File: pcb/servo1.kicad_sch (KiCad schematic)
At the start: 34 parts, among them J1 Feeder 1, J10 Feeder 10, J11 Feeder 11, J12 Feeder 12, J13 Feeder 13, J14 Feeder 14, J15 Feeder 15, J16 Feeder 16, J2 Feeder 2, J3 Feeder 3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

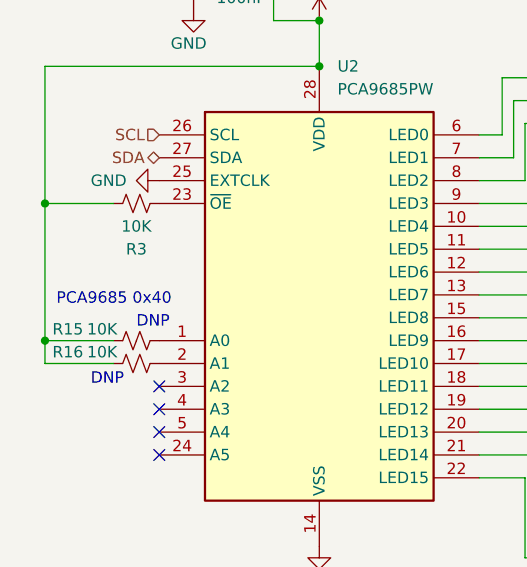
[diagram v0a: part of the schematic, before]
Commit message: Exclude R3 and R9 from population.
Upgrades files to KiCad 7.x.

Fixes: https://github.com/atanisoft/Esp32FeederController/issues/10
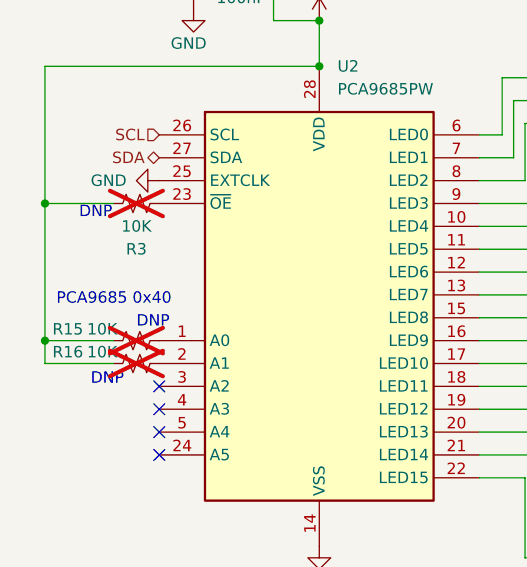
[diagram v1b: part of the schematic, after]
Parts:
- R15, R16, R3: now not fitted; now left out of the parts list
